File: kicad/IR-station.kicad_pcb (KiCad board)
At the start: 2 copper layers, 42 x 42 mm, 29 parts, among them P1 GPIO, P2 USB_Micro_B, Q1 IRLML6344TRPBFTR, SW1 BUTTON, U1 ESP-WROOM-02-2, U2 AE-FT234X, U3 PL-IRM2121, U4 TAR5SB33

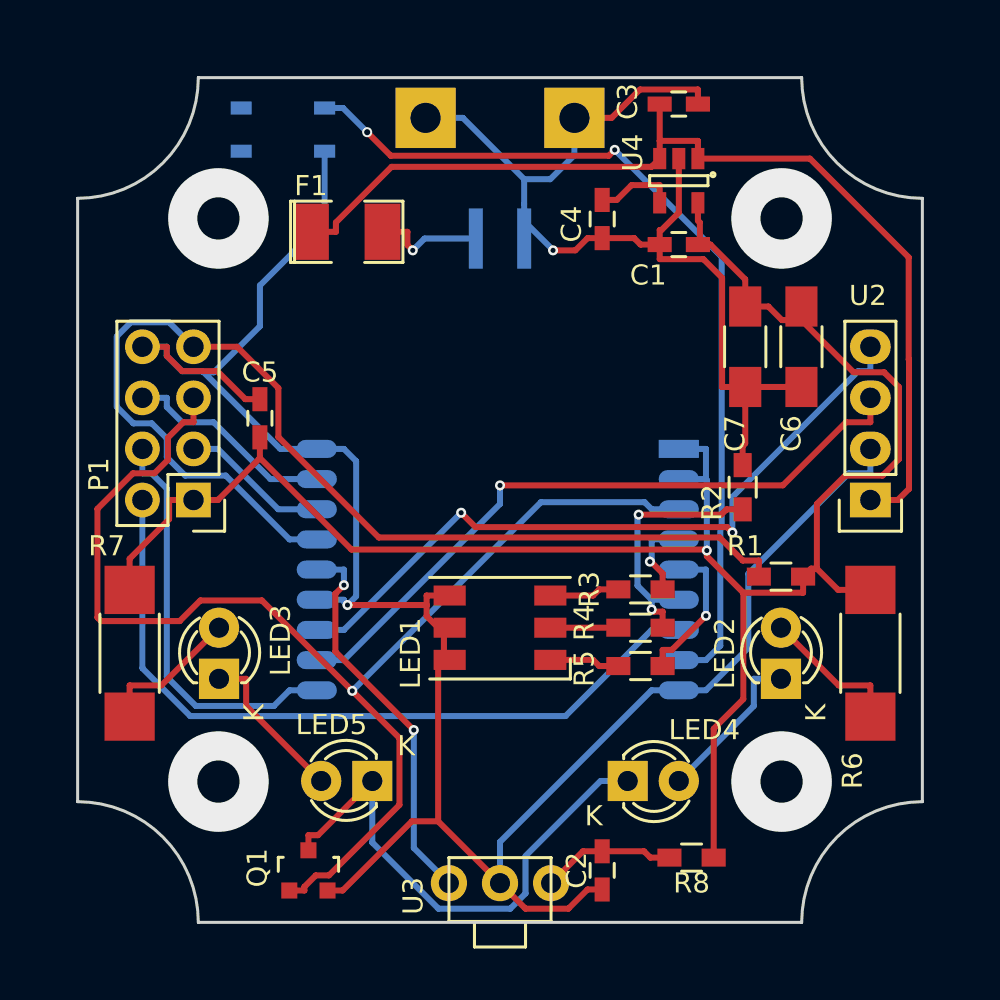
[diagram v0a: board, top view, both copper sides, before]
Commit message: 基板の更新
SHコネクタの使用
AE-FT234Xの使用

2016-09-16 発注済み
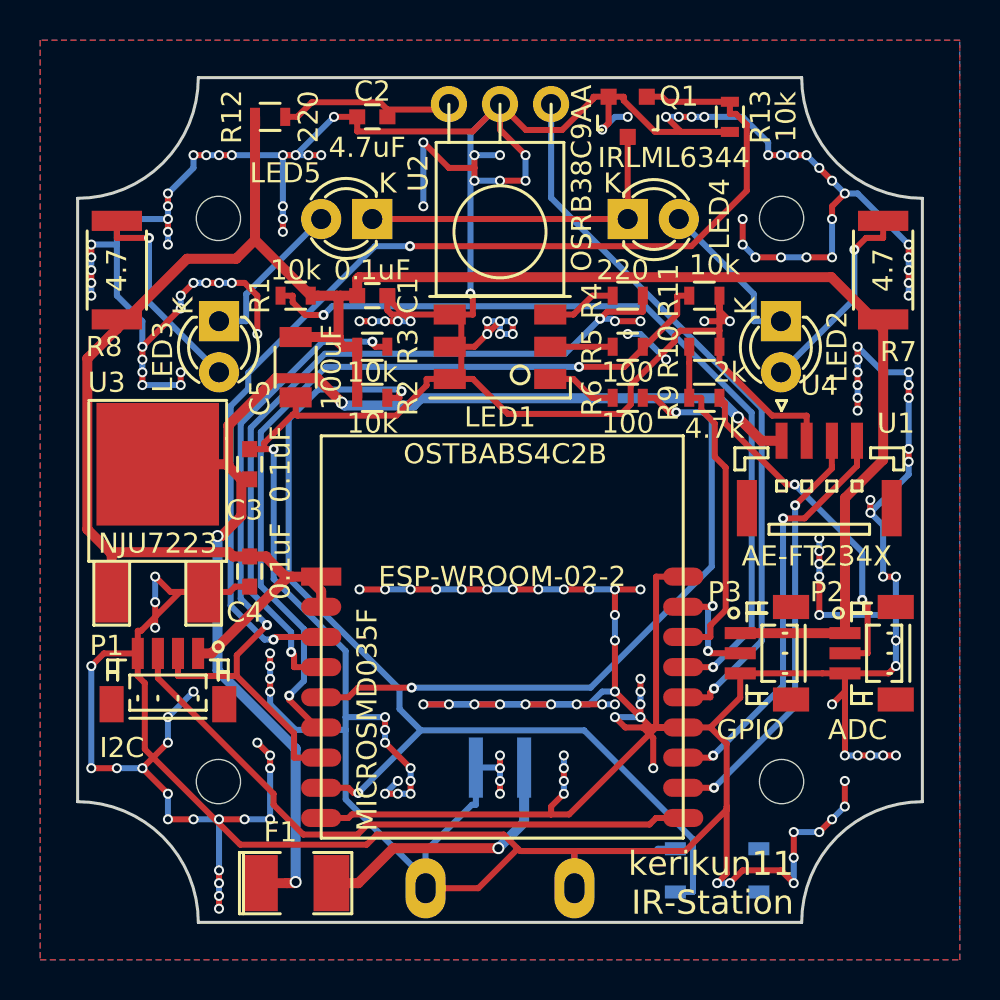
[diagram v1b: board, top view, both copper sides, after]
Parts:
- removed C6, C7: 100uF, Capacitors_SMD:C_1206_HandSoldering
- added G***: LOGO, kerikun11:IR-Station, B.Cu at (100.0, 100.0)
- added H1: MountingHole_2.2mm_M2, Mounting_Holes:MountingHole_2.2mm_M2, F.Cu at (86.0, 86.0)
- added H2: MountingHole_2.2mm_M2, Mounting_Holes:MountingHole_2.2mm_M2, F.Cu at (114.0, 86.0)
- added H3: MountingHole_2.2mm_M2, Mounting_Holes:MountingHole_2.2mm_M2, F.Cu at (114.0, 114.0)
- added H4: MountingHole_2.2mm_M2, Mounting_Holes:MountingHole_2.2mm_M2, F.Cu at (86.0, 114.0)
- added P3: GPIO, Connectors_JST:JST_SH_BM03B-SRSS-TB_03x1.00mm_Straight, F.Cu at (113.2, 107.6)
- added P4: USB_Power, kerikun11:USB_Micro_B_Power, B.Cu at (100.0, 119.3)
- added R10: 2k, Resistors_SMD:R_0603, F.Cu at (110.2, 92.4)
- added R11: 10k, Resistors_SMD:R_0603, F.Cu at (110.2, 89.8)
- added R12: 220, Resistors_SMD:R_0603, F.Cu at (88.6, 81.0)
- added R13: 10k, Resistors_SMD:R_0603, F.Cu at (111.4, 81.0)
- added R9: 4.7k, Resistors_SMD:R_0603, F.Cu at (110.2, 94.9)
- C1, C2, C3: footprint Capacitors_SMD:C_0603_HandSoldering -> Capacitors_SMD:C_0603
- C4: value 0.01uF -> 0.1uF; footprint Capacitors_SMD:C_0603_HandSoldering -> Capacitors_SMD:C_0603
- C5: value 0.1uF -> 100uF; footprint Capacitors_SMD:C_0603_HandSoldering -> Capacitors_SMD:C_1206
- LED1: footprint LEDs:LED_WS2812-PLCC6 -> kerikun11:OSTBABS4C2B
- P1: value GPIO -> I2C; footprint Pin_Headers:Pin_Header_Straight_2x04 -> Connectors_JST:JST_SH_BM04B-SRSS-TB_04x1.00mm_Straight
- P2: value USB_Micro_B -> ADC; footprint My Footprints:USB_Micro_B_Power -> Connectors_JST:JST_SH_BM03B-SRSS-TB_03x1.00mm_Straight; moved to F.Cu
- Q1: value IRLML6344TRPBFTR -> IRLML6344
- R1, R2, R5: footprint Resistors_SMD:R_0603_HandSoldering -> Resistors_SMD:R_0603
- R3: value 220 -> 10k; footprint Resistors_SMD:R_0603_HandSoldering -> Resistors_SMD:R_0603
- R4: value 100 -> 220; footprint Resistors_SMD:R_0603_HandSoldering -> Resistors_SMD:R_0603
- R6: value 4.7 -> 100; footprint Resistors_SMD:R_2010_HandSoldering -> Resistors_SMD:R_0603
- R7: footprint Resistors_SMD:R_2010_HandSoldering -> Resistors_SMD:R_2010
- R8: value 220 -> 4.7; footprint Resistors_SMD:R_0603_HandSoldering -> Resistors_SMD:R_2010
- SW1: footprint My Footprints:SW_PUSH -> kerikun11:SW_PUSH
- U1: footprint My Footprints:ESP-WROOM-02 -> kerikun11:ESP-WROOM-02; moved to F.Cu
- U2: value AE-FT234X -> OSRB38C9AA; footprint Pin_Headers:Pin_Header_Straight_1x04 -> kerikun11:PL-IRMxxxx_Angle
- U3: value PL-IRM2121 -> NJU7223; footprint My Footprints:PL-IRMxxxx -> TO_SOT_Packages_SMD:TO-252-2Lead
- U4: value TAR5SB33 -> AE-FT234X; footprint TO_SOT_Packages_SMD:SOT-23-5 -> Connectors_JST:JST_GH_BM04B-GHS-TBT_04x1.25mm_Straight
- moved SW1 42.7 mm to (110.8, 118.4), turned to 0 degrees
- moved R7 42.0 mm to (119.0, 88.6), turned to 90 degrees
- moved R8 40.9 mm to (81.0, 88.6), turned to 90 degrees
- moved Q1 40.7 mm to (106.3, 81.0), turned to 180 degrees
- moved C2 39.2 mm to (93.7, 81.0), turned to 180 degrees
- moved F1 32.5 mm to (89.8, 119.0)
- moved P2 32.4 mm to (118.4, 107.6), turned to 270 degrees
- moved LED4 27.9 mm to (106.3, 86.0)
- moved LED5 27.9 mm to (93.7, 86.0)
- moved R1 27.9 mm to (89.8, 89.8), turned to 180 degrees
- moved C3 27.9 mm to (87.6, 98.2), turned to 90 degrees
- moved U2 27.0 mm to (100.0, 80.3)
- moved C4 24.8 mm to (87.6, 103.6)
- moved U3 22.3 mm to (83.0, 104.6)
- moved R2 18.9 mm to (93.7, 94.9), turned to 0 degrees
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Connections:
- C4 pad 1: Net-(C4-Pad1) -> +3V3
- F1 pad 2: Net-(F1-Pad2) -> /vbus
- P1 pad 2: GPIO2 -> SDA
- P1 pad 3: ADC -> SCL
- P1 pad 4: GPIO4 -> GND
- P2 pad 1: Net-(F1-Pad2) -> +3V3
- R1 pad 1: RESET -> +3V3
- R1 pad 2: +3V3 -> RESET
- R2 pad 1: LED_G -> +3V3
- R2 pad 2: GND -> BUTTON
- R3 pad 1: LED_R -> +3V3
- R3 pad 2: Net-(LED1-Pad3) -> SDA
- R4 pad 1: LED_G -> LED_R
- R4 pad 2: Net-(LED1-Pad2) -> Net-(LED1-Pad3)
- R5 pad 1: LED_B -> LED_G
- R5 pad 2: Net-(LED1-Pad1) -> Net-(LED1-Pad2)
- R6 pad 1: +3V3 -> LED_B
- R6 pad 2: Net-(LED2-Pad2) -> Net-(LED1-Pad1)
- R7 pad 2: Net-(LED3-Pad2) -> Net-(LED2-Pad2)
- R8 pad 2: Net-(C2-Pad1) -> Net-(LED3-Pad2)
- U1 pad 10: GPIO4 -> SCL
- U1 pad 7: GPIO2 -> SDA
- U2 pad 1: +5V -> IR_IN
- U2 pad 3: RXD -> Net-(C2-Pad1)
- U3 pad 1: IR_IN -> +3V3
- U3 pad 2: GND -> +5V
- U3 pad 3: Net-(C2-Pad1) -> GND
- U4 pad 3: +5V -> RXD
- U4 pad 4: Net-(C4-Pad1) -> TXD
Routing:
- net GND: track 161.0 -> 500.0 mm, vias 2 -> 196
- net GPIO2: track 37.8 -> 0.00 mm
- net LED_R: track 4.16 -> 38.9 mm, vias 1 -> 4
- net SDA: track 0.00 -> 33.5 mm, vias 0 -> 2
- net SCL: track 0.00 -> 31.2 mm
- net LED_G: track 13.0 -> 41.4 mm
- net LED_B: track 7.31 -> 33.3 mm, vias 1 -> 2
- net GPIO4: track 20.5 -> 0.00 mm
- net Net-(P2-Pad2): track 0.00 -> 17.1 mm, vias 0 -> 2
- net IR_IN: track 19.5 -> 36.2 mm, vias 2 -> 1
- net +3V3: track 96.3 -> 112.2 mm, vias 1 -> 0
- net TXD: track 35.9 -> 20.8 mm
- net RESET: track 56.1 -> 41.3 mm, vias 0 -> 2
- net /vbus: track 0.00 -> 13.6 mm, vias 0 -> 1
- net RXD: track 34.2 -> 21.2 mm, vias 1 -> 2
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- added copper zone on B.Cu, net GND
- added copper zone on F.Cu, net GND
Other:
- net class Power added: clearance 0.2, trace_width 0.5, via_dia 0.6, via_drill 0.4
- board text added: "kerikun11 IR-Station"
- board text removed: "kerikun11 IR-Station Ver.1.0.1"

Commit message: 新しく基板を作成
レギュレータを小型のものに変更
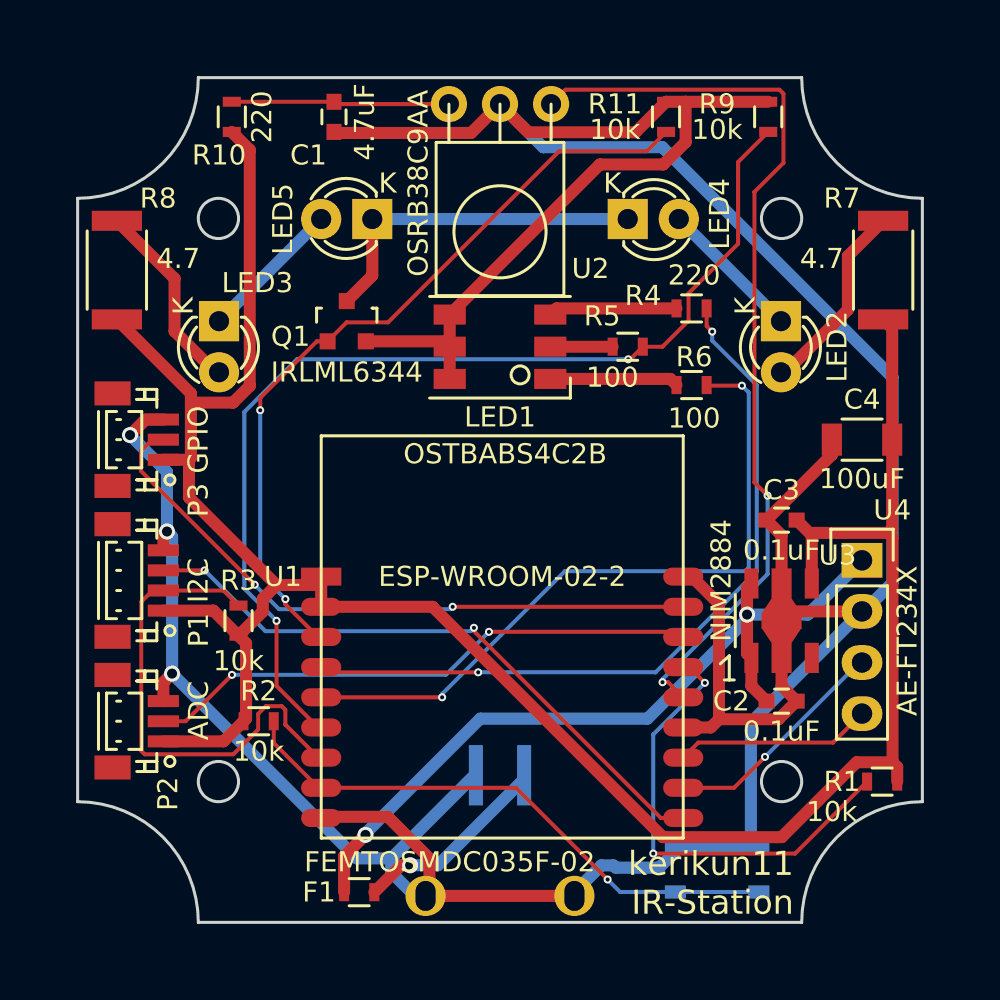
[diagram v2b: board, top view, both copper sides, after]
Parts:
- removed the C1 at (93.7, 89.8)
- removed G***: LOGO, kerikun11:IR-Station
- removed H1, H2, H3, H4: MountingHole_2.2mm_M2, Mounting_Holes:MountingHole_2.2mm_M2
- removed the R10 at (110.2, 92.4)
- removed the R9 at (110.2, 94.9)
- F1: value MICROSMD035F -> FEMTOSMDC035F-02; footprint SMD_Packages:SMD-1210_Pol -> Resistors_SMD:R_0603
- LED1: footprint kerikun11:OSTBABS4C2B -> IR-station:OSTBABS4C2B
- P4: footprint kerikun11:USB_Micro_B_Power -> IR-station:USB_Micro_B_Power
- SW1: footprint kerikun11:SW_PUSH -> IR-station:SW_PUSH
- U1: footprint kerikun11:ESP-WROOM-02 -> IR-station:ESP-WROOM-02
- U2: footprint kerikun11:PL-IRMxxxx_Angle -> IR-station:PL-IRMxxxx_Angle
- U3: value NJU7223 -> NJM2884; footprint TO_SOT_Packages_SMD:TO-252-2Lead -> TO_SOT_Packages_SMD:SOT89-5_Housing
- U4: footprint Connectors_JST:JST_GH_BM04B-GHS-TBT_04x1.25mm_Straight -> Pin_Headers:Pin_Header_Straight_1x04
- moved R1 37.9 mm to (119.0, 114.0)
- moved P2 36.6 mm to (82.0, 111.0), turned to 90 degrees
- moved P3 33.0 mm to (82.0, 97.0), turned to 90 degrees
- moved U3 31.1 mm to (114.0, 106.0)
- moved C2 29.0 mm to (114.0, 110.0), turned to 0 degrees
- moved C4 28.4 mm to (118.0, 97.0), turned to 180 degrees
- moved C3 26.6 mm to (114.0, 101.0), turned to 180 degrees
- moved Q1 17.3 mm to (92.4, 91.1), turned to 0 degrees
- moved R2 17.0 mm to (88.0, 111.0)
- moved R3 15.2 mm to (87.0, 106.0), turned to 90 degrees
- moved R9 9.44 mm to (113.3, 81.0), turned to 90 degrees
- moved P1 5.11 mm to (82.0, 104.0), turned to 90 degrees
- moved U4 4.77 mm to (118.0, 103.0)
- moved R6 3.24 mm to (109.5, 94.3)
- moved R4 3.24 mm to (109.5, 90.5)
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- renumbered C2 to C1, C3 to C2, C4 to C3, C5 to C4, R12 to R10, R13 to R11, R11 to R9
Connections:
- P2 pad 2: Net-(P2-Pad2) -> ADC
- U3 pad 1: +3V3 -> +5V
- U3 pad 2: +5V -> GND
- U3 pad 3: GND -> (no net)
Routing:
- net GND: track 500.0 -> 199.5 mm, vias 196 -> 3
- net GPIO16: track 5.47 -> 32.2 mm
- net BUTTON: track 51.1 -> 28.3 mm, vias 2 -> 1
- net +5V: track 61.0 -> 40.1 mm, vias 4 -> 2
- net RESET: track 41.3 -> 23.1 mm
- net Net-(P2-Pad2): track 17.1 -> 0.00 mm, vias 2 -> 0
- net IR_OUT: track 54.9 -> 38.9 mm
- net TXD: track 20.8 -> 9.80 mm, vias 2 -> 0
- net LED_G: track 41.4 -> 52.4 mm
- net ADC: track 17.2 -> 27.8 mm, vias 0 -> 2
- net RXD: track 21.2 -> 11.5 mm, vias 2 -> 1
- net IR_IN: track 36.2 -> 45.6 mm, vias 1 -> 2
- net SDA: track 33.5 -> 24.7 mm, vias 2 -> 0
- net +3V3: track 112.2 -> 119.7 mm
- net /vbus: track 13.6 -> 9.97 mm
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- removed copper zone on B.Cu, net GND
- removed copper zone on F.Cu, net GND
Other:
- outline, holes or cut-outs redrawn
- net class Default: trace_width 0.3 -> 0.2; via_dia 0.5 -> 0.4
- net class Power: trace_width 0.5 -> 0.6; via_dia 0.6 -> 0.8; via_drill 0.4 -> 0.5

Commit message: 基板にロゴを追加
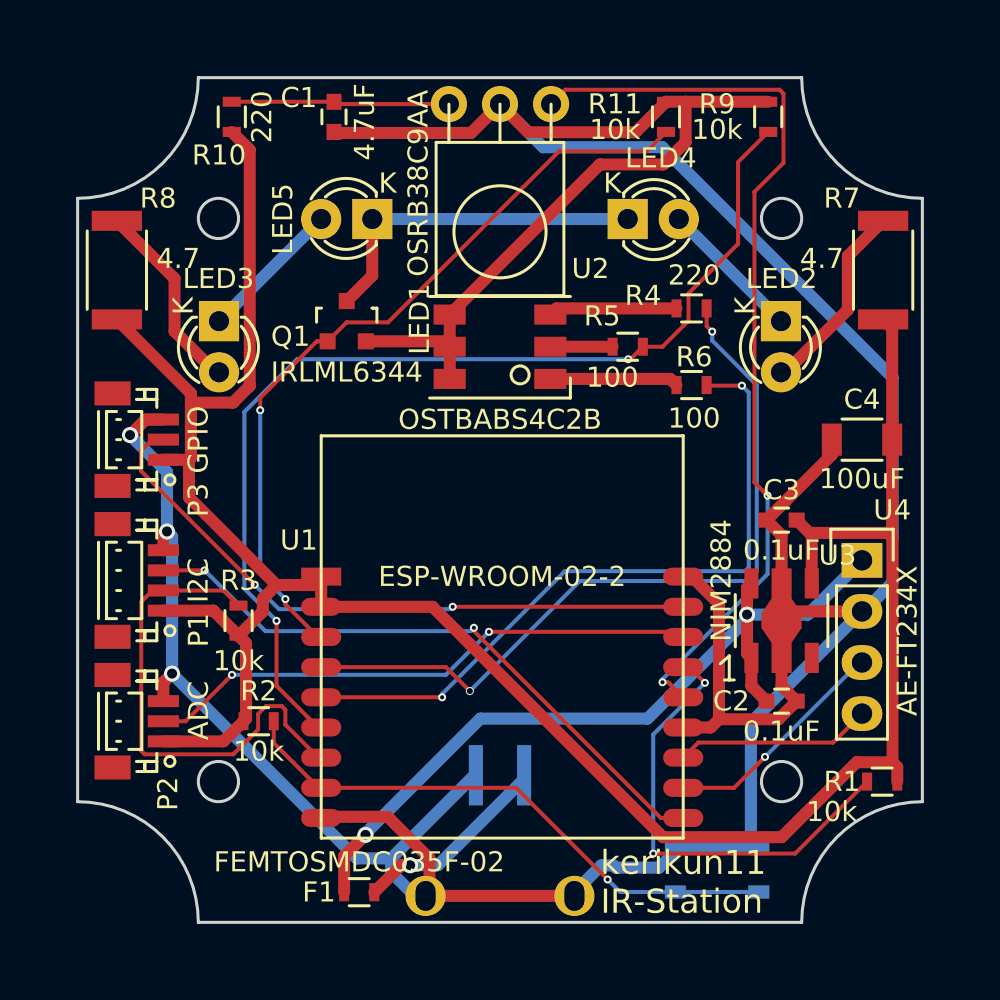
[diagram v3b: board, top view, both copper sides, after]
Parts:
- added G***: LOGO, IR-station:IR-Station, B.Cu at (100.0, 100.0)
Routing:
- net LED_R: track 37.9 -> 39.1 mm
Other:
- board text added: "2017.04.13"
